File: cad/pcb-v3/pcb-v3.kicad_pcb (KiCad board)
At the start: 4 copper layers, 19.3 x 19.3 mm, 50 parts

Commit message: C5 -> 0402 (fixed); found the deeper cause: U5 sits inside the J4 pogo block
C5 IS SETTLED. As an 0603 the whole board offered exactly ONE position with
both pads clear of every pogo ring, and that one is inside the antenna
keep-out, which forbids pads. So C5 is now the SAME 0402 part as C1/C2
(C77000, 10uF 10V) and goes through the packer, which bans GND pads from pogo
rings. 10 V against a 4.30 V cell is ample, and with BT1 on VBAT the cell
dominates the bulk impedance -- C5 handles switching transients, not storage.
One fewer distinct LCSC code as a bonus.

THE CASCADE IS THE INTERESTING PART. Freeing C5 into the 0402 pool changed the
packing, R9 lost the near-U5 slot it had been getting by luck, and PCM_VM came
back with zero copper. Two fixes later -- ordering R9 first, then retargeting
the objective at the PIN rather than the part centre (a real improvement:
U5.3 is at +1.25 in x and R9 had landed at -8.70, so the track had to go the
whole way around a 3.4 mm part) -- PCM_VM still failed.

Because the cause is neither: U5.3 sits 0.461 mm from J4.2, INSIDE its no-via
ring, and U5.4 (S2, GND) is 1.128 mm from a pogo pad. U5 is placed inside the
J4 pogo block. R9 is 2.7k from PCM_VM to GND, so it carries a GND pad and the
new rule correctly bans it from every ring -- it cannot sit beside the pin it
connects to.

U5's position came from ONE objective: minimise S1 -> BT1-2. That drove it to
the bottom-left corner, straight into J4. The search needs a second term --
keep U5.4 out of every ring, and leave a legal 0201 site beside U5.3.

The vault board predates all of today's script changes and remains the
7-open-pad revision with every other check passing. Regenerating before U5's
placement is settled would produce a WORSE board (PCM_VM unrouted), so it is
deliberately not regenerated.
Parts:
- moved R9 17.9 mm to (-8.70, -7.45), turned to 90 degrees
- moved R3 14.4 mm to (-4.30, -7.90)
- moved R8 14.1 mm to (6.05, 2.65)
- moved C5 13.6 mm to (5.00, 3.15), turned to 90 degrees
- moved R6 5.90 mm to (-6.80, -2.65)
- moved R1 5.60 mm to (-3.40, -7.90)
- moved TP3 5.53 mm to (2.53, -0.97)
- moved R7 5.33 mm to (-7.70, -2.65)
- moved C10 2.21 mm to (6.00, 5.84)
- moved C3 1.76 mm to (6.00, 7.60)
- moved C2 0.93 mm to (6.90, 7.85)
- moved C13 0.70 mm to (-2.50, -7.90)
- moved C9 0.70 mm to (1.10, -7.90)
- moved C4 0.70 mm to (2.00, -7.90)
- moved C6 0.70 mm to (0.20, -7.90)
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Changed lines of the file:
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@@
 	(footprint "touchid:TP3"
 		(layer "F.Cu")
-		(at -2.72 -2.72)
+		(at 2.53 -0.97)
 		(property "Reference" "TP3"
 			(at 0 0 0)
@@
 		)
 	)
-	(footprint "touchid:C5"
-		(layer "F.Cu")
-		(at -7.61 -1.92)
-		(property "Reference" "C5"
-			(at 0 0 0)
-			(layer "F.SilkS")
-			(hide yes)
-			(effects (font (size 0.6 0.6) (thickness 0.1)))
-		)
-		(attr smd)
-		(fp_text user "C5"
-			(at 0 0 0)
-			(layer "F.Fab")
-			(effects (font (size 0.4 0.4) (thickness 0.06)))
-		)
-		(pad "1" smd roundrect
-			(at -0.7 0)
-			(size 0.8 0.9)
-			(layers "F.Cu" "F.Mask" "F.Paste")
-			(roundrect_rratio 0.25)
-			(net 23 "VBAT")
-		)
-		(pad "2" smd roundrect
-			(at 0.7 0)
-			(size 0.8 0.9)
-			(layers "F.Cu" "F.Mask" "F.Paste")
-			(roundrect_rratio 0.25)
-			(net 4 "GND")
-		)
-		(model "${KIPRJMOD}/3dmodels/chip_0603.step"
-			(offset (xyz 0 0 0))
-			(scale (xyz 1 1 1))
-			(rotate (xyz 0 0 0))
-		)
-	)
 	(footprint "touchid:L1"
 		(layer "F.Cu")
@@
 	(footprint "touchid:U5"
 		(layer "F.Cu")
-		(at -6.35 -7.9)
+		(at -6.55 -7.9)
 		(property "Reference" "U5"
 			(at 0 0 0)
@@
 		)
 	)
-	(footprint "touchid:R8"
-		(layer "F.Cu")
-		(at -6.75 -3.15)
-		(property "Reference" "R8"
-			(at 0 0 0)
-			(layer "F.SilkS")
-			(hide yes)
-			(effects (font (size 0.6 0.6) (thickness 0.1)))
-		)
-		(attr smd)
-		(fp_text user "R8"
+	(footprint "touchid:R9"
+		(layer "F.Cu")
+		(at -8.7 -7.45 90)
+		(property "Reference" "R9"
+			(at 0 0 0)
+			(layer "F.SilkS")
+			(hide yes)
+			(effects (font (size 0.6 0.6) (thickness 0.1)))
+		)
+		(attr smd)
+		(fp_text user "R9"
 			(at 0 0 0)
 			(layer "F.Fab")
@@
 			(layers "F.Cu" "F.Mask" "F.Paste")
 			(roundrect_rratio 0.25)
-			(net 23 "VBAT")
+			(net 13 "PCM_VM")
 		)
 		(pad "2" smd roundrect
@@
 			(layers "F.Cu" "F.Mask" "F.Paste")
 			(roundrect_rratio 0.25)
-			(net 12 "PCM_VDD")
-		)
-		(model "${KIPRJMOD}/3dmodels/chip_0402.step"
-			(offset (xyz 0 0 0))
-			(scale (xyz 1 1 1))
-			(rotate (xyz 0 0 0))
-		)
-	)
-	(footprint "touchid:R9"
+			(net 4 "GND")
+		)
+		(model "${KIPRJMOD}/3dmodels/chip_0402.step"
+			(offset (xyz 0 0 0))
+			(scale (xyz 1 1 1))
+			(rotate (xyz 0 0 0))
+		)
+	)
+	(footprint "touchid:R8"
 		(layer "F.Cu")
 		(at 6.05 2.65)
-		(property "Reference" "R9"
-			(at 0 0 0)
-			(layer "F.SilkS")
-			(hide yes)
-			(effects (font (size 0.6 0.6) (thickness 0.1)))
-		)
-		(attr smd)
-		(fp_text user "R9"
+		(property "Reference" "R8"
+			(at 0 0 0)
+			(layer "F.SilkS")
+			(hide yes)
+			(effects (font (size 0.6 0.6) (thickness 0.1)))
+		)
+		(attr smd)
+		(fp_text user "R8"
 			(at 0 0 0)
 			(layer "F.Fab")
@@
 			(layers "F.Cu" "F.Mask" "F.Paste")
 			(roundrect_rratio 0.25)
-			(net 13 "PCM_VM")
+			(net 23 "VBAT")
 		)
 		(pad "2" smd roundrect
@@
 			(layers "F.Cu" "F.Mask" "F.Paste")
 			(roundrect_rratio 0.25)
-			(net 4 "GND")
+			(net 12 "PCM_VDD")
 		)
 		(model "${KIPRJMOD}/3dmodels/chip_0402.step"
@@
 	(footprint "touchid:C2"
 		(layer "F.Cu")
+		(at 6.9 7.85 90)
+		(property "Reference" "C2"
+			(at 0 0 0)
+			(layer "F.SilkS")
+			(hide yes)
+			(effects (font (size 0.6 0.6) (thickness 0.1)))
+		)
+		(attr smd)
+		(fp_text user "C2"
+			(at 0 0 0)
+			(layer "F.Fab")
+			(effects (font (size 0.4 0.4) (thickness 0.06)))
+		)
+		(pad "1" smd roundrect
+			(at -0.42 0)
+			(size 0.5 0.54)
+			(layers "F.Cu" "F.Mask" "F.Paste")
+			(roundrect_rratio 0.25)
+			(net 30 "VSTOR")
+		)
+		(pad "2" smd roundrect
+			(at 0.42 0)
+			(size 0.5 0.54)
+			(layers "F.Cu" "F.Mask" "F.Paste")
+			(roundrect_rratio 0.25)
+			(net 4 "GND")
+		)
+		(model "${KIPRJMOD}/3dmodels/chip_0402.step"
+			(offset (xyz 0 0 0))
+			(scale (xyz 1 1 1))
+			(rotate (xyz 0 0 0))
+		)
+	)
+	(footprint "touchid:C3"
+		(layer "F.Cu")
 		(at 6.0 7.6 90)
-		(property "Reference" "C2"
-			(at 0 0 0)
-			(layer "F.SilkS")
-			(hide yes)
-			(effects (font (size 0.6 0.6) (thickness 0.1)))
-		)
-		(attr smd)
-		(fp_text user "C2"
+		(property "Reference" "C3"
+			(at 0 0 0)
+			(layer "F.SilkS")
+			(hide yes)
+			(effects (font (size 0.6 0.6) (thickness 0.1)))
+		)
+		(attr smd)
+		(fp_text user "C3"
 			(at 0 0 0)
 			(layer "F.Fab")
@@
 		)
 	)
-	(footprint "touchid:C3"
-		(layer "F.Cu")
-		(at 6.0 5.836 90)
-		(property "Reference" "C3"
-			(at 0 0 0)
-			(layer "F.SilkS")
-			(hide yes)
-			(effects (font (size 0.6 0.6) (thickness 0.1)))
-		)
-		(attr smd)
-		(fp_text user "C3"
-			(at 0 0 0)
-			(layer "F.Fab")
-			(effects (font (size 0.4 0.4) (thickness 0.06)))
-		)
-		(pad "1" smd roundrect
-			(at -0.42 0)
-			(size 0.5 0.54)
-			(layers "F.Cu" "F.Mask" "F.Paste")
-			(roundrect_rratio 0.25)
-			(net 30 "VSTOR")
-		)
-		(pad "2" smd roundrect
-			(at 0.42 0)
-			(size 0.5 0.54)
-			(layers "F.Cu" "F.Mask" "F.Paste")
-			(roundrect_rratio 0.25)
-			(net 4 "GND")
-		)
-		(model "${KIPRJMOD}/3dmodels/chip_0402.step"
-			(offset (xyz 0 0 0))
-			(scale (xyz 1 1 1))
-			(rotate (xyz 0 0 0))
-		)
-	)
 	(footprint "touchid:C4"
 		(layer "F.Cu")
-		(at 1.3 -7.9 90)
+		(at 2.0 -7.9 90)
 		(property "Reference" "C4"
 			(at 0 0 0)
@@
 		)
 	)
+	(footprint "touchid:C5"
+		(layer "F.Cu")
+		(at 5.0 3.15 90)
+		(property "Reference" "C5"
+			(at 0 0 0)
+			(layer "F.SilkS")
+			(hide yes)
+			(effects (font (size 0.6 0.6) (thickness 0.1)))
+		)
+		(attr smd)
+		(fp_text user "C5"
+			(at 0 0 0)
+			(layer "F.Fab")
+			(effects (font (size 0.4 0.4) (thickness 0.06)))
+		)
+		(pad "1" smd roundrect
+			(at -0.42 0)
+			(size 0.5 0.54)
+			(layers "F.Cu" "F.Mask" "F.Paste")
+			(roundrect_rratio 0.25)
+			(net 23 "VBAT")
+		)
+		(pad "2" smd roundrect
+			(at 0.42 0)
+			(size 0.5 0.54)
+			(layers "F.Cu" "F.Mask" "F.Paste")
+			(roundrect_rratio 0.25)
+			(net 4 "GND")
+		)
+		(model "${KIPRJMOD}/3dmodels/chip_0603.step"
+			(offset (xyz 0 0 0))
+			(scale (xyz 1 1 1))
+			(rotate (xyz 0 0 0))
+		)
+	)
 	(footprint "touchid:C6"
 		(layer "F.Cu")
-		(at -0.5 -7.9 90)
+		(at 0.2 -7.9 90)
 		(property "Reference" "C6"
 			(at 0 0 0)
@@
 	(footprint "touchid:C9"
 		(layer "F.Cu")
-		(at 0.4 -7.9 90)
+		(at 1.1 -7.9 90)
 		(property "Reference" "C9"
 			(at 0 0 0)
@@
 	(footprint "touchid:C10"
 		(layer "F.Cu")
-		(at 6.9 7.85 90)
+		(at 6.0 5.836 90)
 		(property "Reference" "C10"
 			(at 0 0 0)
@@
 	(footprint "touchid:C12"
 		(layer "F.Cu")
-		(at -2.3 -7.9 90)
+		(at -1.6 -7.9 90)
 		(property "Reference" "C12"
 			(at 0 0 0)
@@
 	(footprint "touchid:C13"
 		(layer "F.Cu")
-		(at -3.2 -7.9 90)
+		(at -2.5 -7.9 90)
 		(property "Reference" "C13"
 			(at 0 0 0)
@@
 	(footprint "touchid:R1"
 		(layer "F.Cu")
-		(at 2.2 -7.9 90)
+		(at -3.4 -7.9 90)
 		(property "Reference" "R1"
 			(at 0 0 0)
@@
 	(footprint "touchid:R2"
 		(layer "F.Cu")
-		(at 3.1 -7.9 90)
+		(at 2.9 -7.9 90)
 		(property "Reference" "R2"
 			(at 0 0 0)
@@
 	(footprint "touchid:R3"
 		(layer "F.Cu")
-		(at 5.0 3.15 90)
+		(at -4.3 -7.9 90)
 		(property "Reference" "R3"
 			(at 0 0 0)
@@
 	(footprint "touchid:R4"
 		(layer "F.Cu")
-		(at -8.2 -3.05)
+		(at -8.6 -2.65 90)
 		(property "Reference" "R4"
 			(at 0 0 0)
@@
 	(footprint "touchid:R5"
 		(layer "F.Cu")
-		(at -1.4 -7.9 90)
+		(at -0.7 -7.9 90)
 		(property "Reference" "R5"
 			(at 0 0 0)
@@
 	(footprint "touchid:R6"
 		(layer "F.Cu")
-		(at -4.1 -7.9 90)
+		(at -6.8 -2.65 90)
 		(property "Reference" "R6"
 			(at 0 0 0)
@@
 	(footprint "touchid:R7"
 		(layer "F.Cu")
-		(at -8.6 -7.9 90)
+		(at -7.7 -2.65 90)
 		(property "Reference" "R7"
 			(at 0 0 0)

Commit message: U5 placement gains a second objective; PCM_VM routes, board rebuilt clean
U5's position came from ONE term -- minimise S1 -> BT1-2 -- and that drove it
into the bottom-left corner and straight into the J4 pogo block: U5.3 (V-) was
0.461 mm from J4.2, inside its no-via ring, and U5.4 (S2, GND) 1.128 mm from a
pogo pad. Fatal twice. S2 returns every milliamp on the board and needs a solid
path to the plane, which no ring permits. And R9 is 2.7k from PCM_VM to GND, so
it carries a GND pad and the ring ban correctly kept it away from the pin it
connects to -- PCM_VM routed with zero copper.

The trial loop now rejects any U5 position where S2 sits in a ring or V- has no
legal neighbourhood, as cheap point tests before the expensive packer trial.

  U5 -> (-4.65,-7.90), S1->BT1-2 = 2.85 mm (was 2.28 into the pogo block)
  stage 1 routing        9/9 SUCCESS, PCM_VM included
  nets with copper       29 of 30, only GND empty as intended
  0402 packer            23/23

Board rebuilt end to end from the fixed script and finished properly: GND pours
cloned onto F.Cu and B.Cu at 0.10 clearance (not the plane's 0.25, which was
the mistake last time), and the one dangling stub removed by looping on
preflight's own report.

  check_board   0 different-net pairs closer than 0.10
  sexp_check    PARSE OK, 17 zones, 697 segments, 101 vias
  blockers      6 (8 open pads), 17 and 18 -- and 17/18 are the fill

Trading 0.57 mm of cell path for a PCM that is out of the pogo block and whose
sense leg can reach its own pin is clearly the right side of that bargain.
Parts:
- moved C12 7.00 mm to (-8.60, -7.90)
- moved R1 5.50 mm to (2.10, -7.90)
- moved R3 3.40 mm to (-7.70, -7.90)
- moved C10 2.21 mm to (6.90, 7.85)
- moved R9 1.90 mm to (-6.80, -7.45)
- moved U5 1.90 mm to (-4.65, -7.90)
- moved C3 1.76 mm to (6.00, 5.84)
- moved C2 0.93 mm to (6.00, 7.60)
- moved C4 0.80 mm to (1.20, -7.90)
- moved C6 0.80 mm to (-0.60, -7.90)
- moved C9 0.80 mm to (0.30, -7.90)
- moved R5 0.80 mm to (-1.50, -7.90)
- moved C13 0.10 mm to (-2.40, -7.90)
- moved R2 0.10 mm to (3.00, -7.90)
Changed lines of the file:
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@@
 	(footprint "touchid:U5"
 		(layer "F.Cu")
-		(at -6.55 -7.9)
+		(at -4.65 -7.9)
 		(property "Reference" "U5"
 			(at 0 0 0)
@@
 	(footprint "touchid:R9"
 		(layer "F.Cu")
-		(at -8.7 -7.45 90)
+		(at -6.8 -7.45 90)
 		(property "Reference" "R9"
 			(at 0 0 0)
@@
 	(footprint "touchid:C2"
 		(layer "F.Cu")
-		(at 6.9 7.85 90)
+		(at 6.0 7.6 90)
 		(property "Reference" "C2"
 			(at 0 0 0)
@@
 	(footprint "touchid:C3"
 		(layer "F.Cu")
-		(at 6.0 7.6 90)
+		(at 6.0 5.836 90)
 		(property "Reference" "C3"
 			(at 0 0 0)
@@
 	(footprint "touchid:C4"
 		(layer "F.Cu")
-		(at 2.0 -7.9 90)
+		(at 1.2 -7.9 90)
 		(property "Reference" "C4"
 			(at 0 0 0)
@@
 	(footprint "touchid:C6"
 		(layer "F.Cu")
-		(at 0.2 -7.9 90)
+		(at -0.6 -7.9 90)
 		(property "Reference" "C6"
 			(at 0 0 0)
@@
 	(footprint "touchid:C9"
 		(layer "F.Cu")
-		(at 1.1 -7.9 90)
+		(at 0.3 -7.9 90)
 		(property "Reference" "C9"
 			(at 0 0 0)
@@
 	(footprint "touchid:C10"
 		(layer "F.Cu")
-		(at 6.0 5.836 90)
+		(at 6.9 7.85 90)
 		(property "Reference" "C10"
 			(at 0 0 0)
@@
 	(footprint "touchid:C12"
 		(layer "F.Cu")
-		(at -1.6 -7.9 90)
+		(at -8.6 -7.9 90)
 		(property "Reference" "C12"
 			(at 0 0 0)
@@
 	(footprint "touchid:C13"
 		(layer "F.Cu")
-		(at -2.5 -7.9 90)
+		(at -2.4 -7.9 90)
 		(property "Reference" "C13"
 			(at 0 0 0)
@@
 	(footprint "touchid:R1"
 		(layer "F.Cu")
-		(at -3.4 -7.9 90)
+		(at 2.1 -7.9 90)
 		(property "Reference" "R1"
 			(at 0 0 0)
@@
 	(footprint "touchid:R2"
 		(layer "F.Cu")
-		(at 2.9 -7.9 90)
+		(at 3.0 -7.9 90)
 		(property "Reference" "R2"
 			(at 0 0 0)
@@
 	(footprint "touchid:R3"
 		(layer "F.Cu")
-		(at -4.3 -7.9 90)
+		(at -7.7 -7.9 90)
 		(property "Reference" "R3"
 			(at 0 0 0)
@@
 	(footprint "touchid:R5"
 		(layer "F.Cu")
-		(at -0.7 -7.9 90)
+		(at -1.5 -7.9 90)
 		(property "Reference" "R5"
 			(at 0 0 0)

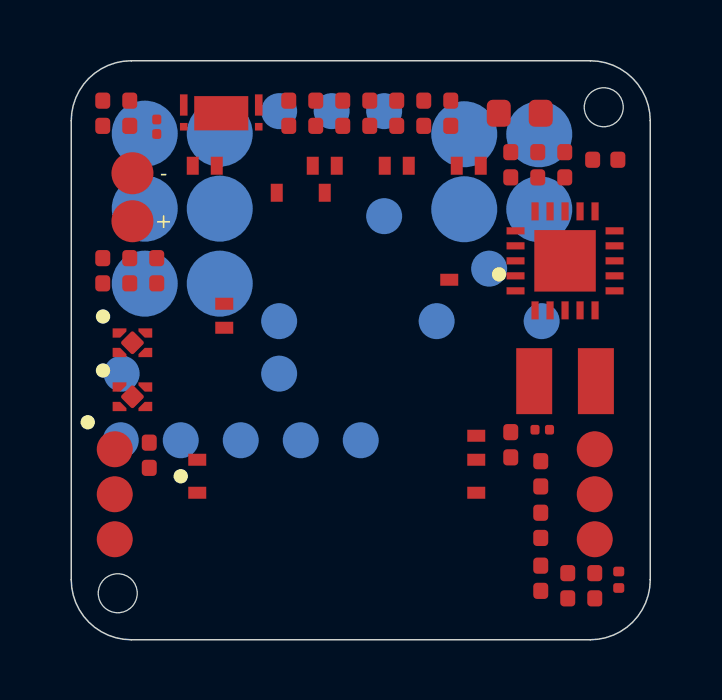
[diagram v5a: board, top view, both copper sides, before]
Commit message: REVERT the last two placement rules -- correct alone, worse together
Added: the 0201 placer honouring pogo rings for GND pads (R9 carries one), and
U5's V- clearing every ring by 0.30 mm. Each fixes something real.

Together they pushed U5 to 3.39 mm from the cell pad and R9 to 13.3 mm from U5,
and the rebuild came out at 15 open pads, 5 dangling ends and a DRC violation --
against 8 open pads and everything else clean on the board already in the vault.

Reverted build_pcb_v3.py to the revision that produced the good board. The rules
are written into ROUTING-V4-STATUS.md instead, with the reason they cannot just
be re-added: U5 must simultaneously keep S1 near BT1-2, give V- a ring-free
neighbourhood for R9, keep S2 out of every ring, and leave the packer room for
23 passives. That is a four-way constraint, and the search currently optimises
one term with rejections bolted on. It needs a real cost function.

Also recorded the decisive measurement from gnd_via_anchor.py: ALL 41 GND pads
already have a via within 2.5 mm. The remaining opens are therefore not about
via proximity -- they are pour connectivity, and KiCad's own DRC is the
authority on that and has never been run. That is the next step, not more
surgery from this side.
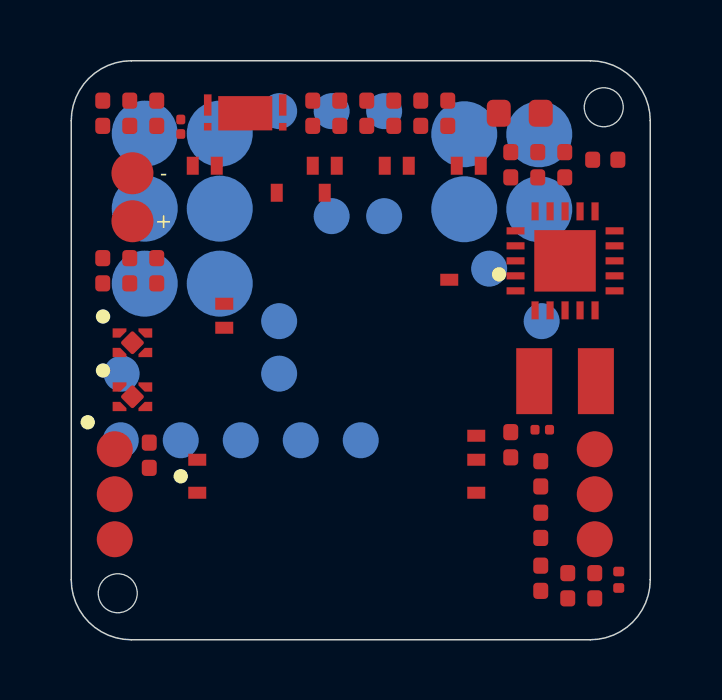
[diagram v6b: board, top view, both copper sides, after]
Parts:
- moved R5 17.2 mm to (6.00, 7.60)
- moved R9 16.3 mm to (6.05, 2.65), turned to 0 degrees
- moved R8 15.7 mm to (-6.00, -7.45), turned to 90 degrees
- moved C5 12.4 mm to (-0.70, -7.90)
- moved R1 8.90 mm to (-6.80, -7.90)
- moved C10 5.07 mm to (5.00, 3.15)
- moved TP3 4.95 mm to (-0.97, -4.47)
- moved C3 2.21 mm to (6.90, 7.85)
- moved C2 1.76 mm to (6.00, 5.84)
- moved U5 0.80 mm to (-3.85, -7.90)
- moved C4 0.80 mm to (2.00, -7.90)
- moved C6 0.80 mm to (0.20, -7.90)
- moved C9 0.80 mm to (1.10, -7.90)
- moved C13 0.80 mm to (-1.60, -7.90)
- moved R2 0.10 mm to (2.90, -7.90)
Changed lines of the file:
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@@
 	(footprint "touchid:TP3"
 		(layer "F.Cu")
-		(at 2.53 -0.97)
+		(at -0.97 -4.47)
 		(property "Reference" "TP3"
 			(at 0 0 0)
@@
 	(footprint "touchid:U5"
 		(layer "F.Cu")
-		(at -4.65 -7.9)
+		(at -3.85 -7.9)
 		(property "Reference" "U5"
 			(at 0 0 0)
@@
 	(footprint "touchid:R9"
 		(layer "F.Cu")
-		(at -6.8 -7.45 90)
+		(at 6.05 2.65)
 		(property "Reference" "R9"
 			(at 0 0 0)
@@
 	(footprint "touchid:R8"
 		(layer "F.Cu")
-		(at 6.05 2.65)
+		(at -6.0 -7.45 90)
 		(property "Reference" "R8"
 			(at 0 0 0)
@@
 	(footprint "touchid:C2"
 		(layer "F.Cu")
-		(at 6.0 7.6 90)
+		(at 6.0 5.836 90)
 		(property "Reference" "C2"
 			(at 0 0 0)
@@
 	(footprint "touchid:C3"
 		(layer "F.Cu")
-		(at 6.0 5.836 90)
+		(at 6.9 7.85 90)
 		(property "Reference" "C3"
 			(at 0 0 0)
@@
 	(footprint "touchid:C4"
 		(layer "F.Cu")
-		(at 1.2 -7.9 90)
+		(at 2.0 -7.9 90)
 		(property "Reference" "C4"
 			(at 0 0 0)
@@
 	(footprint "touchid:C5"
 		(layer "F.Cu")
-		(at 5.0 3.15 90)
+		(at -0.7 -7.9 90)
 		(property "Reference" "C5"
 			(at 0 0 0)
@@
 	(footprint "touchid:C6"
 		(layer "F.Cu")
-		(at -0.6 -7.9 90)
+		(at 0.2 -7.9 90)
 		(property "Reference" "C6"
 			(at 0 0 0)
@@
 	(footprint "touchid:C9"
 		(layer "F.Cu")
-		(at 0.3 -7.9 90)
+		(at 1.1 -7.9 90)
 		(property "Reference" "C9"
 			(at 0 0 0)
@@
 	(footprint "touchid:C10"
 		(layer "F.Cu")
-		(at 6.9 7.85 90)
+		(at 5.0 3.15 90)
 		(property "Reference" "C10"
 			(at 0 0 0)
@@
 	(footprint "touchid:C13"
 		(layer "F.Cu")
-		(at -2.4 -7.9 90)
+		(at -1.6 -7.9 90)
 		(property "Reference" "C13"
 			(at 0 0 0)
@@
 	(footprint "touchid:R1"
 		(layer "F.Cu")
-		(at 2.1 -7.9 90)
+		(at -6.8 -7.9 90)
 		(property "Reference" "R1"
 			(at 0 0 0)
@@
 	(footprint "touchid:R2"
 		(layer "F.Cu")
-		(at 3.0 -7.9 90)
+		(at 2.9 -7.9 90)
 		(property "Reference" "R2"
 			(at 0 0 0)
@@
 	(footprint "touchid:R5"
 		(layer "F.Cu")
-		(at -1.5 -7.9 90)
+		(at 6.0 7.6 90)
 		(property "Reference" "R5"
 			(at 0 0 0)
